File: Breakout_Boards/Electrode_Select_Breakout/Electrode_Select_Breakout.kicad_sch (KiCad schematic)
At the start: 3 parts, among them J1 Conn_01x06_Pin, J2 2xRJ_45, J3 Conn_01x06_Pin

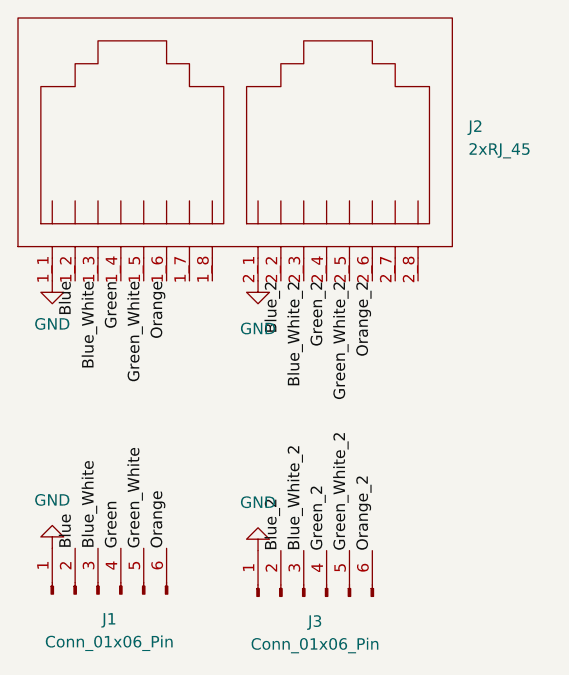
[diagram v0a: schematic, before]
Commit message: Create an electrode select breakout board
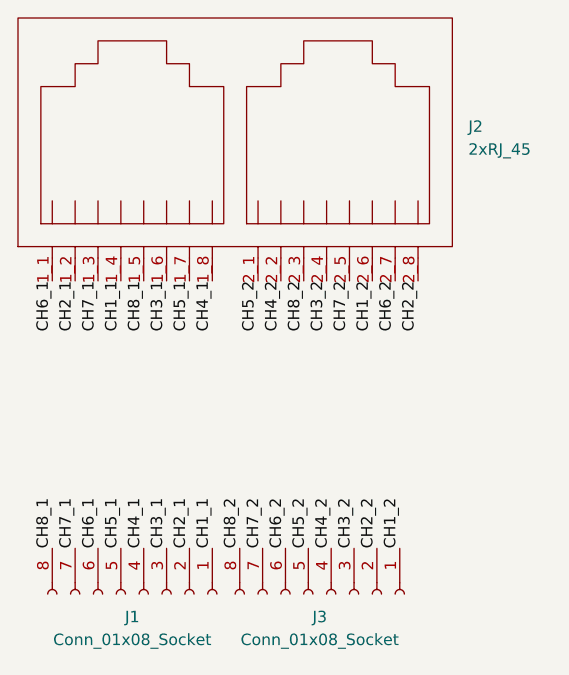
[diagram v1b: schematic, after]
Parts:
- removed J1, J3: Conn_01x06_Pin, Connector_PinSocket_2.54mm:PinSocket_1x06_P2.54mm_Vertical, symbol Connector:Conn_01x06_Pin
- added J1, J3: Conn_01x08_Socket, Connector_PinSocket_2.54mm:PinSocket_1x08_P2.54mm_Vertical, symbol Connector:Conn_01x08_Socket
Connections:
- net CH5_1: now reaches J2.1_7
- net CH5_1: now also J1.5 (Pin_5)
- net CH4_1: now reaches J2.1_8
- net CH4_1: now also J1.4 (Pin_4)
- net CH6_2: now reaches J2.2_7
- net CH6_2: now also J3.6 (Pin_6)
- net CH2_2: now reaches J2.2_8
- net CH2_2: now also J3.2 (Pin_2)
- net Blue renamed CH2_1
- net CH2_1: now also J1.2 (Pin_2)
- net Blue_2 renamed CH4_2
- net CH4_2: now also J3.4 (Pin_4)
- net Blue_White renamed CH7_1
- net CH7_1: now also J1.7 (Pin_7)
- net Blue_White_2 renamed CH8_2
- net CH8_2: now also J3.8 (Pin_8)
- net GND renamed CH5_2
- net CH5_2: now also J3.5 (Pin_5); no longer J2.1_1
- net Green renamed CH1_1
- net CH1_1: now also J1.1 (Pin_1)
- net Green_2 renamed CH3_2
- net CH3_2: now also J3.3 (Pin_3)
- net Green_White renamed CH8_1
- net CH8_1: now also J1.8 (Pin_8)
- net Green_White_2 renamed CH7_2
- net CH7_2: now also J3.7 (Pin_7)
- net Orange renamed CH3_1
- net CH3_1: now also J1.3 (Pin_3)
- net Orange_2 renamed CH1_2
- net CH1_2: now also J3.1 (Pin_1)
- new net CH6_1: J1.6 (Pin_6), J2.1_1
